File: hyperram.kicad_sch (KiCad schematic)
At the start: 7 parts, among them U11 S27KL0641DABHI023

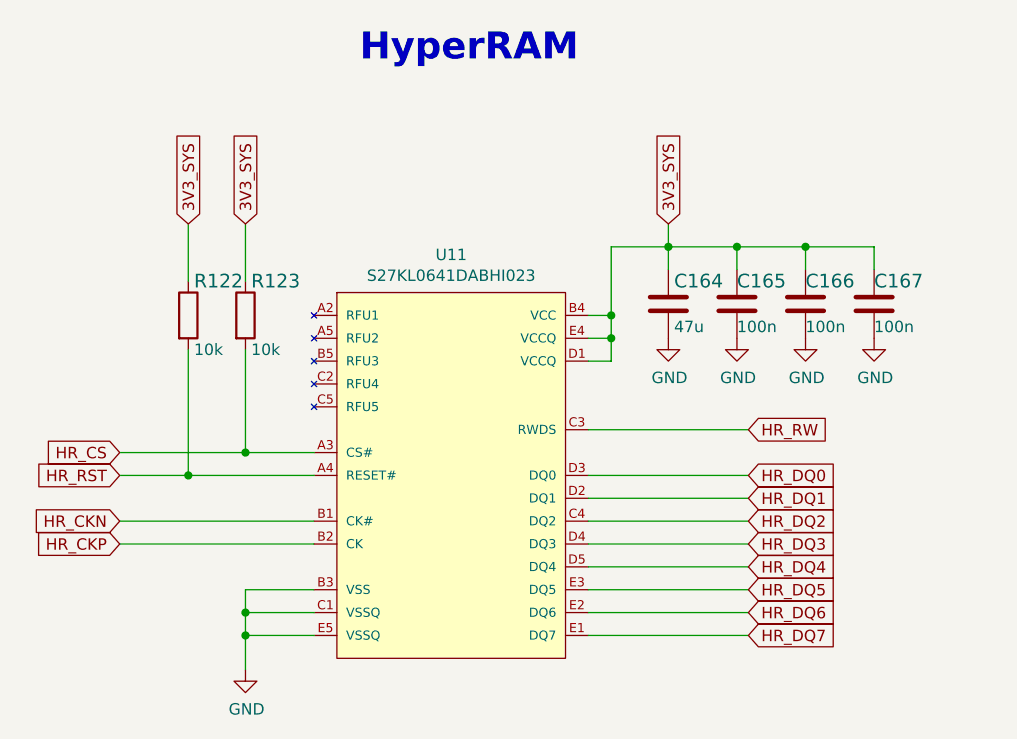
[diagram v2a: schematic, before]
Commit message: Introduce component standarization
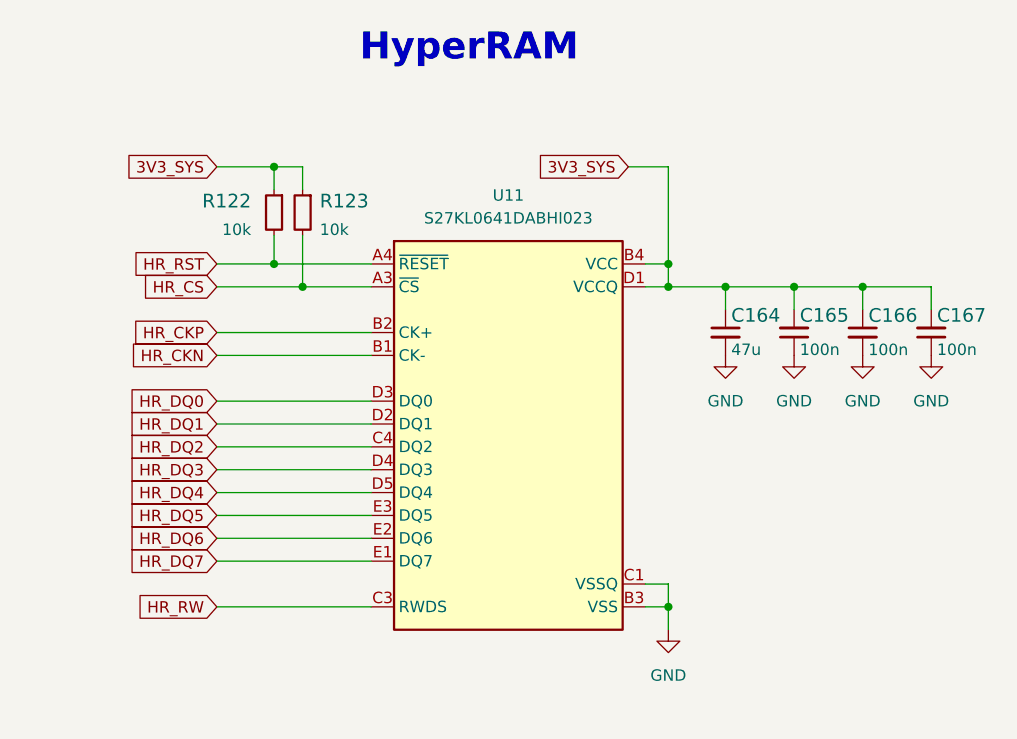
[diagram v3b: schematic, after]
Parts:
- C164: footprint data-center-rdimm-ddr5-tester-footprints:0603-cap -> data-center-rdimm-ddr5-tester-footprints:C_0603_1608Metric; Author (none) -> Antmicro; License (none) -> Apache-2.0; Manufacturer MURATA -> Murata
- C165, C166, C167: value C_100n_0402_6V3 -> C_100n_6V3_0402; footprint data-center-rdimm-ddr5-tester-footprints:0402-cap -> data-center-rdimm-ddr5-tester-footprints:C_0402_1005Metric; symbol data-center-rdimm-ddr5-tester:C_100n_0402_6V3 -> data-center-rdimm-ddr5-tester:C_100n_6V3_0402; Author (none) -> Antmicro; License (none) -> Apache-2.0
- R122, R123: footprint data-center-rdimm-ddr5-tester-footprints:0402-res -> data-center-rdimm-ddr5-tester-footprints:R_0402_1005Metric; Author (none) -> Antmicro; License (none) -> Apache-2.0; MPN CRCW040210K0FKEDHP -> CR0402-FX-1002GLF; Manufacturer VISHAY -> Bourns; Tolerance (none) -> 1%
- U11: footprint data-center-rdimm-ddr5-tester-footprints:FBGA-24 -> data-center-rdimm-ddr5-tester-footprints:FBGA-24-1_6x8mm_Layout5x5_P1mm; Author (none) -> Antmicro; License (none) -> Apache-2.0; Manufacturer CYPRESS SEMICONDUCTOR -> Cypress Semiconductor
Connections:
- net 3V3_SYS: now also C165.2, C167.2; no longer C165.1, C167.1
- net GND: now also C165.1, C167.1; no longer C165.2, C167.2
- net at U11.A2 (NC): now also U11.A5 (NC), U11.B5 (NC), U11.C2 (NC), U11.C5 (NC)
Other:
- moved on the sheet: C164, C165, C166, C167, R122, R123

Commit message: [#55296] component update
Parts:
- U11: footprint data-center-rdimm-ddr5-tester-footprints:FBGA-24-1_6x8mm_Layout5x5_P1mm -> data-center-rdimm-ddr5-tester-footprints:FBGA-25-24_6x8mm_Layout5x5_P1mm
